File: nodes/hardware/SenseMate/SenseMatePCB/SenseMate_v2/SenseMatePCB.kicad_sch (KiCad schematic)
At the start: 19 parts, among them J1 Conn_01x04, J2 Conn_01x12_Pin, J3 Conn_Coaxial, J4 Conn_01x06_Pin, J5 Conn_01x06_Pin, J6 Conn_01x02_Pin, M1 Motor_DC, Q1 2SC1815, Q2 2SC1815, SW5 SW_DPDT_x2, U1 XIAO-nRF52840-Plus-SMD, U2 RFM95W-868S2

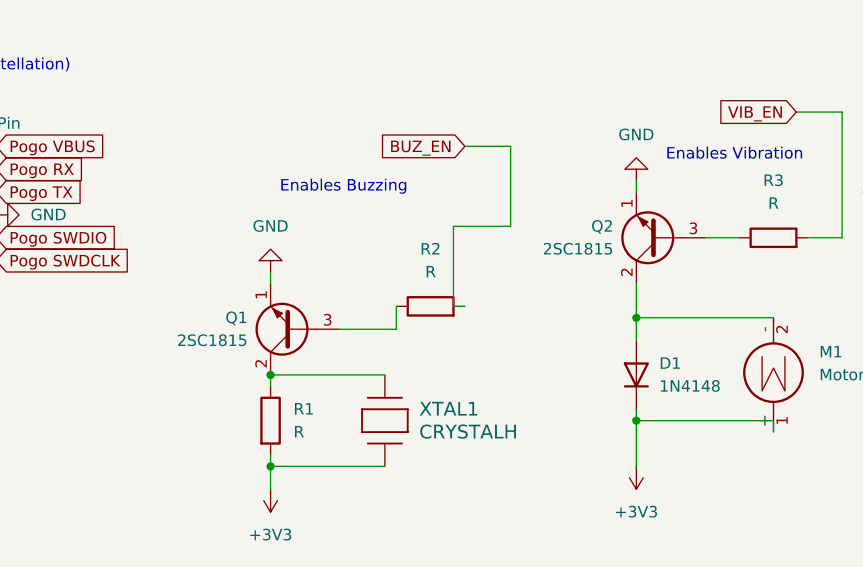
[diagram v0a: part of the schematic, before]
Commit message: Changed SMD Transistor to SS8050 to fix Problem with wrong fields
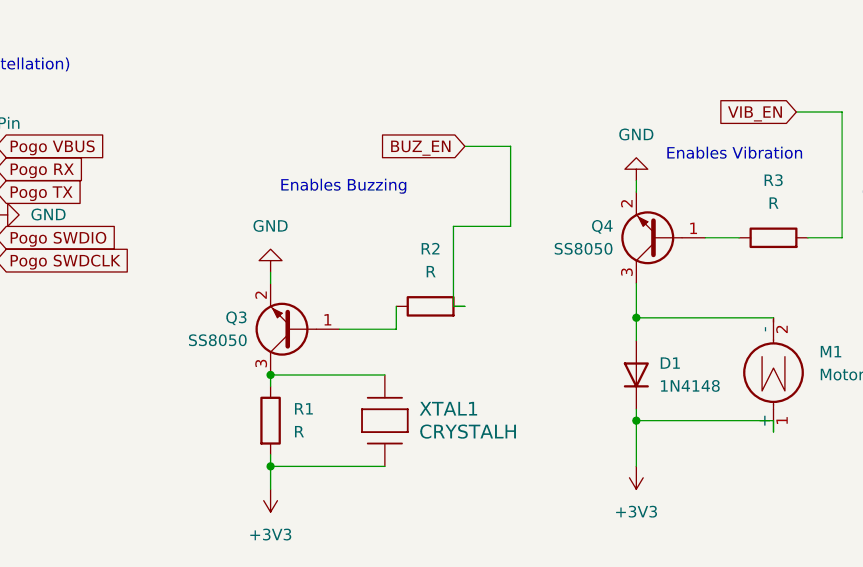
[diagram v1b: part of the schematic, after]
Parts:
- removed Q1, Q2: 2SC1815, Package_TO_SOT_SMD:SOT-23, symbol Transistor_BJT:2SC1815
- added Q3, Q4: SS8050, Package_TO_SOT_SMD:SOT-23, symbol Transistor_BJT:SS8050
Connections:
- net GND: now also Q3.2 (E), Q4.2 (E)
- net at R1.1, XTAL1.2: now also Q3.3 (C)
- net at R2.1: now also Q3.1 (B)
- net at D1.2 (A), M1.2 (-): now also Q4.3 (C)
- net at R3.1: now also Q4.1 (B)
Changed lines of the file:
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@@
 	)
 	(junction
+		(at 110.49 160.02)
+		(diameter 0)
+		(color 0 0 0 0)
+	)
+	(junction
 		(at 62.23 111.76)
 		(diameter 0)
@@
 		(color 0 0 0 0)
 	)
-	(junction
-		(at 110.49 160.02)
-		(diameter 0)
-		(color 0 0 0 0)
-	)
 	(no_connect
 		(at 166.37 86.36)
@@
 	)
 	(symbol
-		(lib_id "Transistor_BJT:2SC1815")
-		(at 113.03 154.94 180)
-		(unit 1)
-		(body_style 1)
-		(exclude_from_sim no)
-		(in_bom yes)
-		(on_board yes)
-		(in_pos_files yes)
-		(dnp no)
-		(fields_autoplaced yes)
-		(property "Reference" "Q1"
-			(at 107.95 153.6699 0)
-			(show_name no)
-			(do_not_autoplace no)
-			(effects
-				(font
-					(size 1.27 1.27)
-				)
-				(justify left)
-			)
-		)
-		(property "Value" "2SC1815"
-			(at 107.95 156.2099 0)
-			(show_name no)
-			(do_not_autoplace no)
-			(effects
-				(font
-					(size 1.27 1.27)
-				)
-				(justify left)
-			)
-		)
-		(property "Footprint" "Package_TO_SOT_SMD:SOT-23"
-			(at 107.95 153.035 0)
-			(hide yes)
-			(show_name no)
-			(do_not_autoplace no)
-			(effects
-				(font
-					(size 1.27 1.27)
-					(italic yes)
-				)
-				(justify left)
-			)
-		)
-		(property "Datasheet" "https://media.digikey.com/pdf/Data%20Sheets/Toshiba%20PDFs/2SC1815.pdf"
-			(at 113.03 154.94 0)
-			(hide yes)
-			(show_name no)
-			(do_not_autoplace no)
-			(effects
-				(font
-					(size 1.27 1.27)
-				)
-				(justify left)
-			)
-		)
-		(property "Description" "0.15A Ic, 50V Vce, Low Noise Audio NPN Transistor, TO-92"
-			(at 113.03 154.94 0)
-			(hide yes)
-			(show_name no)
-			(do_not_autoplace no)
-			(effects
-				(font
-					(size 1.27 1.27)
-				)
-			)
-		)
-		(pin "2"
-		)
-		(pin "1"
-		)
-		(pin "3"
-		)
-		(instances
-			(project "SenseMatePCB"
-				(path "/70e40189-008f-4f72-8f4c-fe289f3548a4"
-					(reference "Q1")
-					(unit 1)
-				)
-			)
-		)
-	)
-	(symbol
 		(lib_id "power:GND")
 		(at 39.37 139.7 90)
@@
 	)
 	(symbol
+		(lib_id "Transistor_BJT:SS8050")
+		(at 113.03 154.94 180)
+		(unit 1)
+		(body_style 1)
+		(exclude_from_sim no)
+		(in_bom yes)
+		(on_board yes)
+		(in_pos_files yes)
+		(dnp no)
+		(fields_autoplaced yes)
+		(property "Reference" "Q3"
+			(at 107.95 153.6699 0)
+			(show_name no)
+			(do_not_autoplace no)
+			(effects
+				(font
+					(size 1.27 1.27)
+				)
+				(justify left)
+			)
+		)
+		(property "Value" "SS8050"
+			(at 107.95 156.2099 0)
+			(show_name no)
+			(do_not_autoplace no)
+			(effects
+				(font
+					(size 1.27 1.27)
+				)
+				(justify left)
+			)
+		)
+		(property "Footprint" "Package_TO_SOT_SMD:SOT-23"
+			(at 107.95 147.574 0)
+			(hide yes)
+			(show_name no)
+			(do_not_autoplace no)
+			(effects
+				(font
+					(size 1.27 1.27)
+					(italic yes)
+				)
+				(justify left)
+			)
+		)
+		(property "Datasheet" "http://www.secosgmbh.com/datasheet/products/SSMPTransistor/SOT-23/SS8050.pdf"
+			(at 107.95 150.114 0)
+			(hide yes)
+			(show_name no)
+			(do_not_autoplace no)
+			(effects
+				(font
+					(size 1.27 1.27)
+				)
+				(justify left)
+			)
+		)
+		(property "Description" "General Purpose NPN Transistor, 1.5A Ic, 25V Vce, SOT-23"
+			(at 78.994 152.654 0)
+			(hide yes)
+			(show_name no)
+			(do_not_autoplace no)
+			(effects
+				(font
+					(size 1.27 1.27)
+				)
+			)
+		)
+		(property "Sim.Device" "NPN"
+			(at 113.03 154.94 0)
+			(hide yes)
+			(show_name no)
+			(do_not_autoplace no)
+			(effects
+				(font
+					(size 1.27 1.27)
+				)
+			)
+		)
+		(property "Sim.Pins" "1=B 2=E 3=C"
+			(at 113.03 154.94 0)
+			(hide yes)
+			(show_name no)
+			(do_not_autoplace no)
+			(effects
+				(font
+					(size 1.27 1.27)
+				)
+			)
+		)
+		(pin "1"
+		)
+		(pin "3"
+		)
+		(pin "2"
+		)
+		(instances
+			(project "SenseMatePCB"
+				(path "/70e40189-008f-4f72-8f4c-fe289f3548a4"
+					(reference "Q3")
+					(unit 1)
+				)
+			)
+		)
+	)
+	(symbol
 		(lib_id "Connector:Conn_Coaxial")
 		(at 196.85 29.21 0)
@@
 	)
 	(symbol
+		(lib_id "Transistor_BJT:SS8050")
+		(at 153.67 144.78 180)
+		(unit 1)
+		(body_style 1)
+		(exclude_from_sim no)
+		(in_bom yes)
+		(on_board yes)
+		(in_pos_files yes)
+		(dnp no)
+		(fields_autoplaced yes)
+		(property "Reference" "Q4"
+			(at 148.59 143.5099 0)
+			(show_name no)
+			(do_not_autoplace no)
+			(effects
+				(font
+					(size 1.27 1.27)
+				)
+				(justify left)
+			)
+		)
+		(property "Value" "SS8050"
+			(at 148.59 146.0499 0)
+			(show_name no)
+			(do_not_autoplace no)
+			(effects
+				(font
+					(size 1.27 1.27)
+				)
+				(justify left)
+			)
+		)
+		(property "Footprint" "Package_TO_SOT_SMD:SOT-23"
+			(at 148.59 137.414 0)
+			(hide yes)
+			(show_name no)
+			(do_not_autoplace no)
+			(effects
+				(font
+					(size 1.27 1.27)
+					(italic yes)
+				)
+				(justify left)
+			)
+		)
+		(property "Datasheet" "http://www.secosgmbh.com/datasheet/products/SSMPTransistor/SOT-23/SS8050.pdf"
+			(at 148.59 139.954 0)
+			(hide yes)
+			(show_name no)
+			(do_not_autoplace no)
+			(effects
+				(font
+					(size 1.27 1.27)
+				)
+				(justify left)
+			)
+		)
+		(property "Description" "General Purpose NPN Transistor, 1.5A Ic, 25V Vce, SOT-23"
+			(at 119.634 142.494 0)
+			(hide yes)
+			(show_name no)
+			(do_not_autoplace no)
+			(effects
+				(font
+					(size 1.27 1.27)
+				)
+			)
+		)
+		(property "Sim.Device" "NPN"
+			(at 153.67 144.78 0)
+			(hide yes)
+			(show_name no)
+			(do_not_autoplace no)
+			(effects
+				(font
+					(size 1.27 1.27)
+				)
+			)
+		)
+		(property "Sim.Pins" "1=B 2=E 3=C"
+			(at 153.67 144.78 0)
+			(hide yes)
+			(show_name no)
+			(do_not_autoplace no)
+			(effects
+				(font
+					(size 1.27 1.27)
+				)
+			)
+		)
+		(pin "3"
+		)
+		(pin "1"
+		)
+		(pin "2"
+		)
+		(instances
+			(project "SenseMatePCB"
+				(path "/70e40189-008f-4f72-8f4c-fe289f3548a4"
+					(reference "Q4")
+					(unit 1)
+				)
+			)
+		)
+	)
+	(symbol
 		(lib_id "power:GND")
 		(at 191.77 152.4 0)
@@
 					(unit 1)
 				)
-			)
-		)
-	)
-	(symbol
-		(lib_id "Transistor_BJT:2SC1815")
-		(at 153.67 144.78 180)
-		(unit 1)
-		(body_style 1)
-		(exclude_from_sim no)
-		(in_bom yes)
-		(on_board yes)
-		(in_pos_files yes)
-		(dnp no)
-		(fields_autoplaced yes)
-		(property "Reference" "Q2"
-			(at 148.59 143.5099 0)
-			(show_name no)
-			(do_not_autoplace no)
-			(effects
-				(font
-					(size 1.27 1.27)
-				)
-				(justify left)
-			)
-		)
-		(property "Value" "2SC1815"
-			(at 148.59 146.0499 0)
-			(show_name no)
-			(do_not_autoplace no)
-			(effects
-				(font
-					(size 1.27 1.27)
-				)
-				(justify left)
-			)
-		)
-		(property "Footprint" "Package_TO_SOT_SMD:SOT-23"
-			(at 148.59 142.875 0)
-			(hide yes)
-			(show_name no)
-			(do_not_autoplace no)
-			(effects
-				(font
-					(size 1.27 1.27)
-					(italic yes)
-				)
-				(justify left)
-			)
-		)
-		(property "Datasheet" "https://media.digikey.com/pdf/Data%20Sheets/Toshiba%20PDFs/2SC1815.pdf"
-			(at 153.67 144.78 0)
-			(hide yes)
-			(show_name no)
-			(do_not_autoplace no)
-			(effects
-				(font
-					(size 1.27 1.27)
-				)
-				(justify left)
-			)
-		)
-		(property "Description" "0.15A Ic, 50V Vce, Low Noise Audio NPN Transistor, TO-92"
-			(at 153.67 144.78 0)
-			(hide yes)
-			(show_name no)
-			(do_not_autoplace no)
-			(effects
-				(font
-					(size 1.27 1.27)
-				)
-			)
-		)
-		(pin "3"
-		)
-		(pin "2"
-		)
-		(pin "1"
-		)
-		(instances
-			(project "SenseMatePCB"
-				(path "/70e40189-008f-4f72-8f4c-fe289f3548a4"
-					(reference "Q2")
-					(unit 1)
-				)

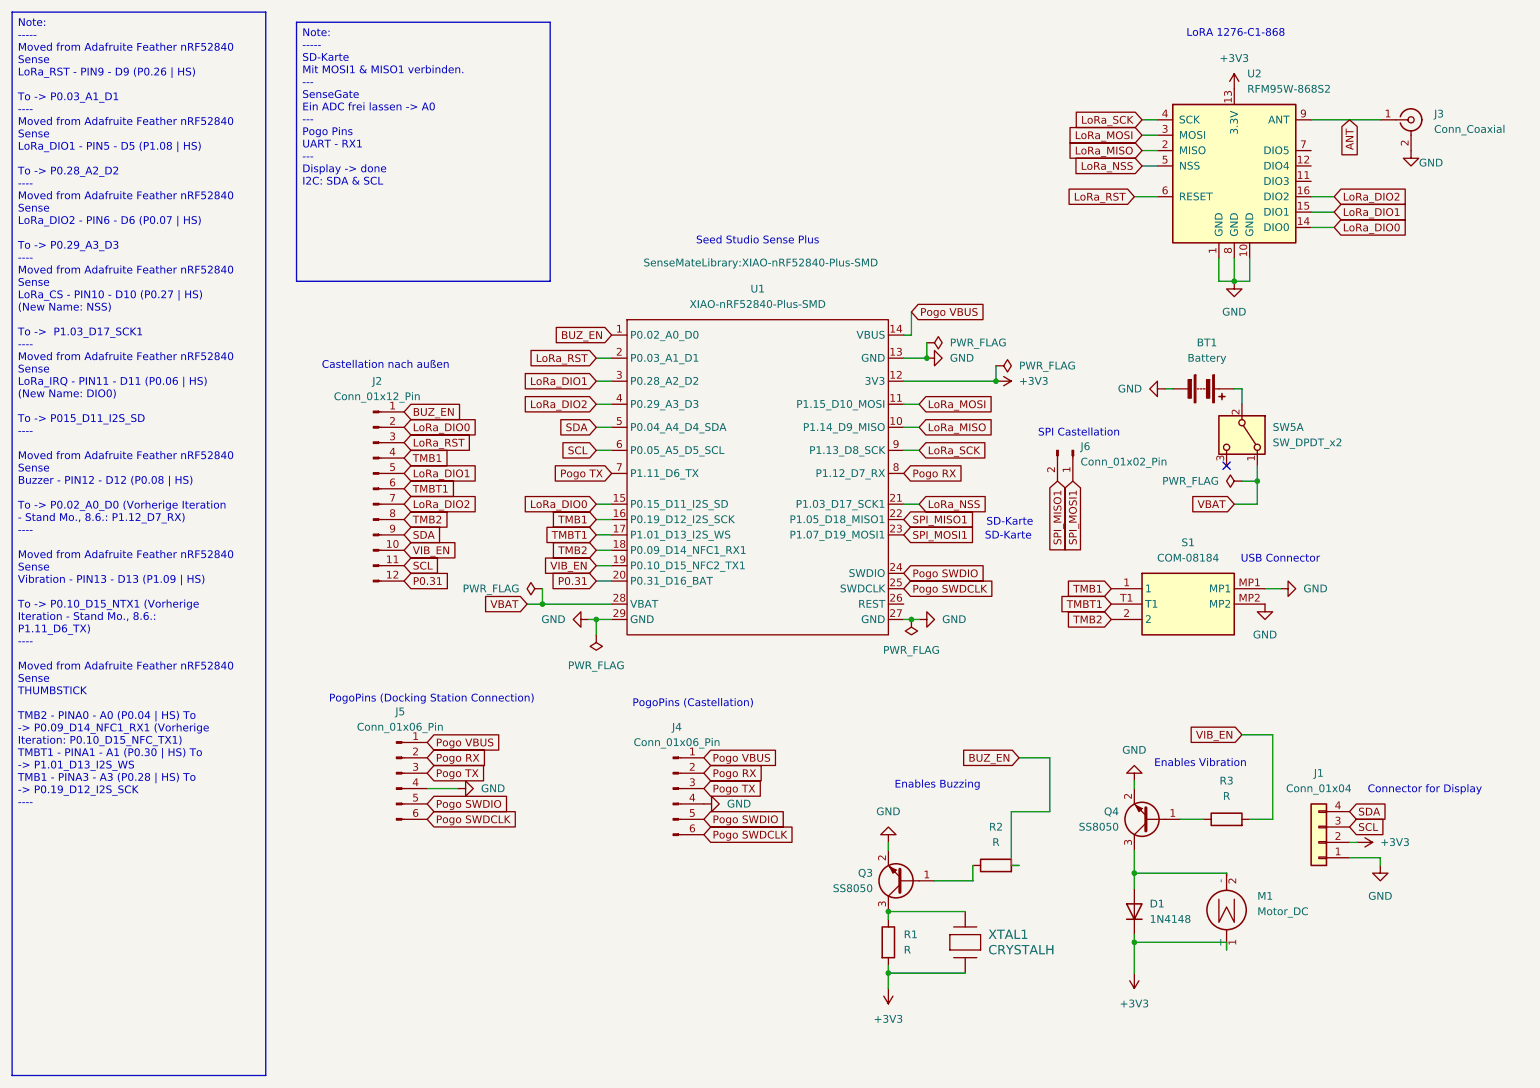
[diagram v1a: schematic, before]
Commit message: pass power to outside with castellation and some minor tweaks to traces
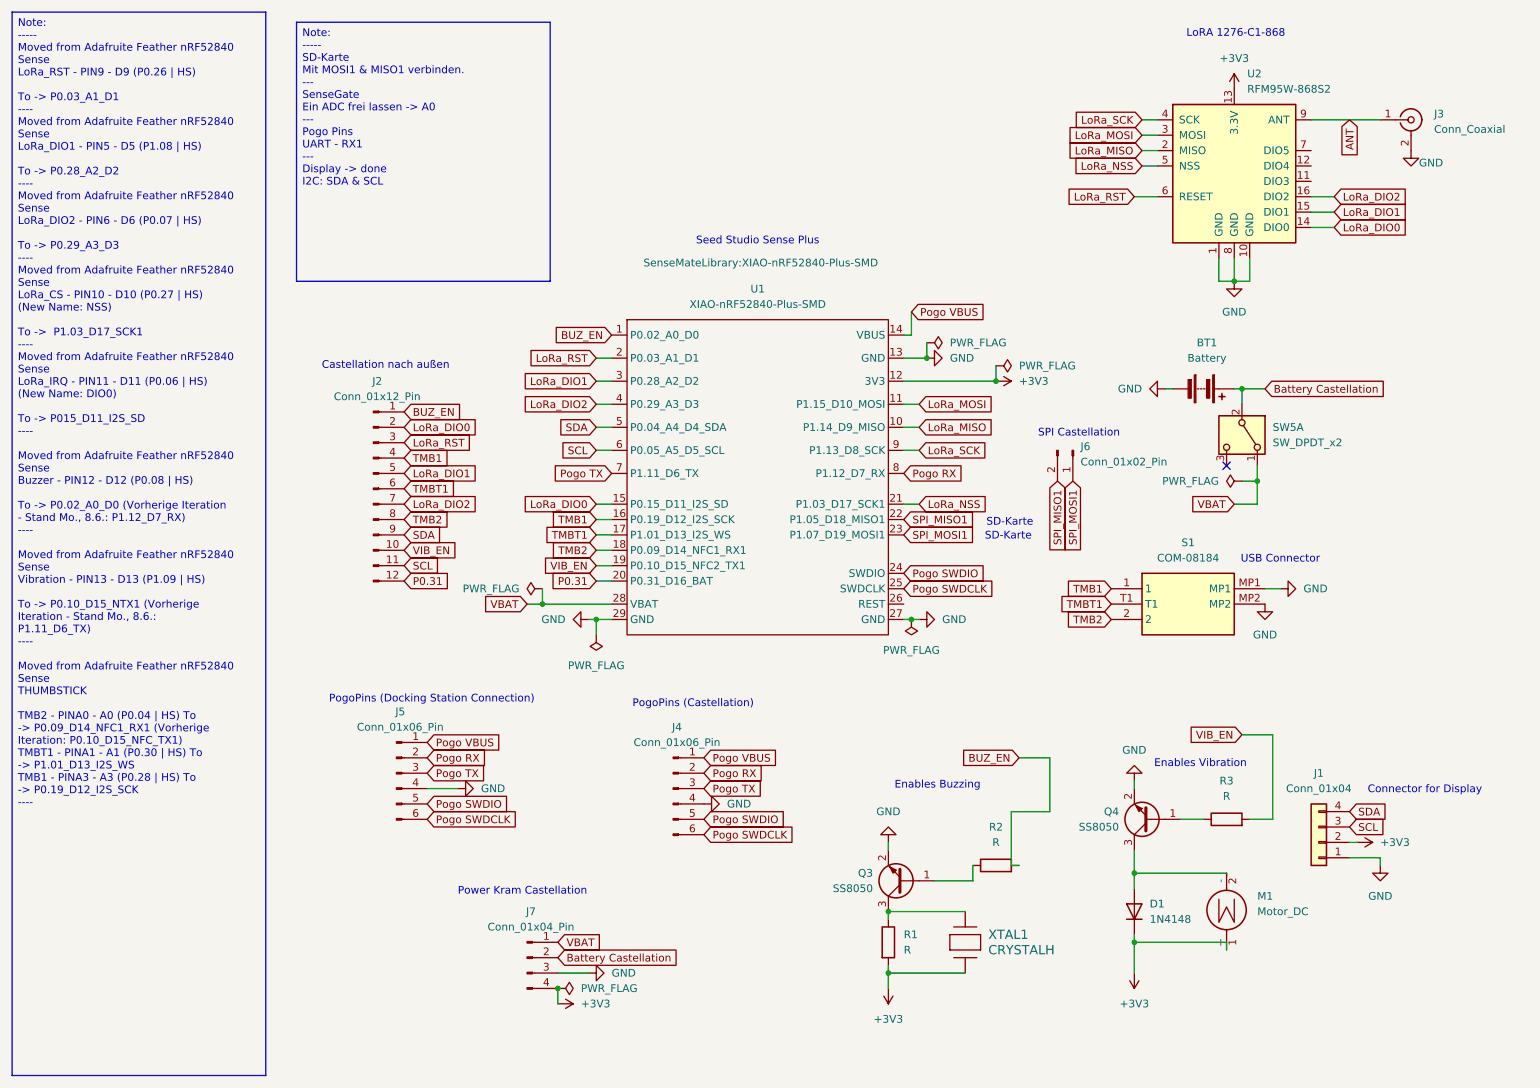
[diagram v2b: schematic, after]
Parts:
- added J7: Conn_01x04_Pin, SenseGateLibrary:Castellated_1x4_2.00mm, symbol Connector:Conn_01x04_Pin
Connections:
- net +3V3: now also J7.4 (Pin_4)
- net GND: now also J7.3 (Pin_3)
- net VBAT: now also J7.1 (Pin_1)
- net Battery Castellation: now reaches BT1.1 (+), SW5.2 (B)
- net Battery Castellation: now also J7.2 (Pin_2)
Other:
- note added: "Power Kram Castellation"
